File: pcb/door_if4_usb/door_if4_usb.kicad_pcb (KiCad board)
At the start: 4 copper layers, 90 x 45 mm, 117 parts, among them J1 WAGO 250-206, J2 WAGO 250-206, J3 WAGO 250-206, Q1 IRF7343, Q2 IRF7343, Q3 IRF7343, Q4 IRF7343, Q5 IRF7343, Q6 IRF7343, U1 Pico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

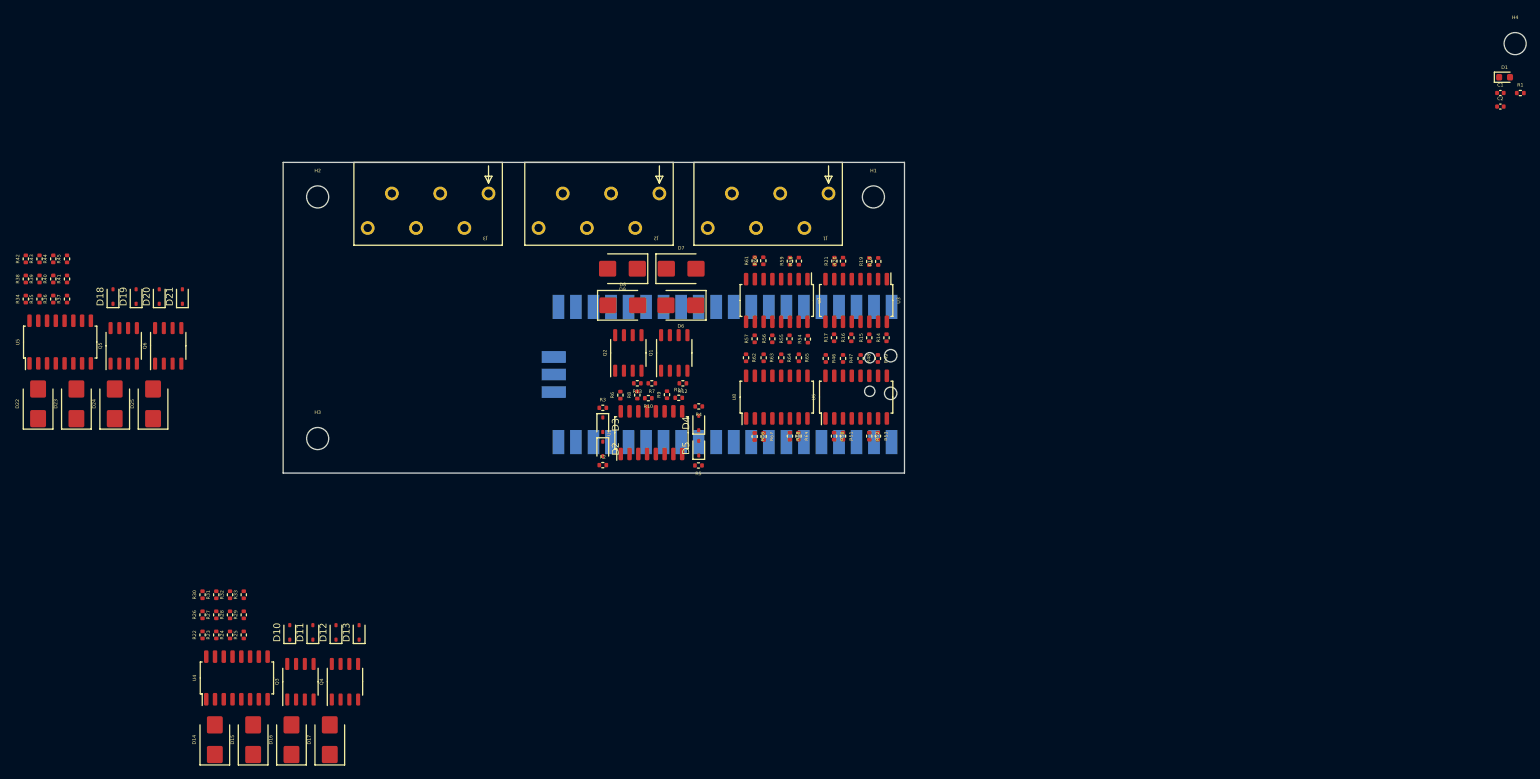
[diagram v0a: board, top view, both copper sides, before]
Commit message: almost completed door_if4_usb for manufacturing
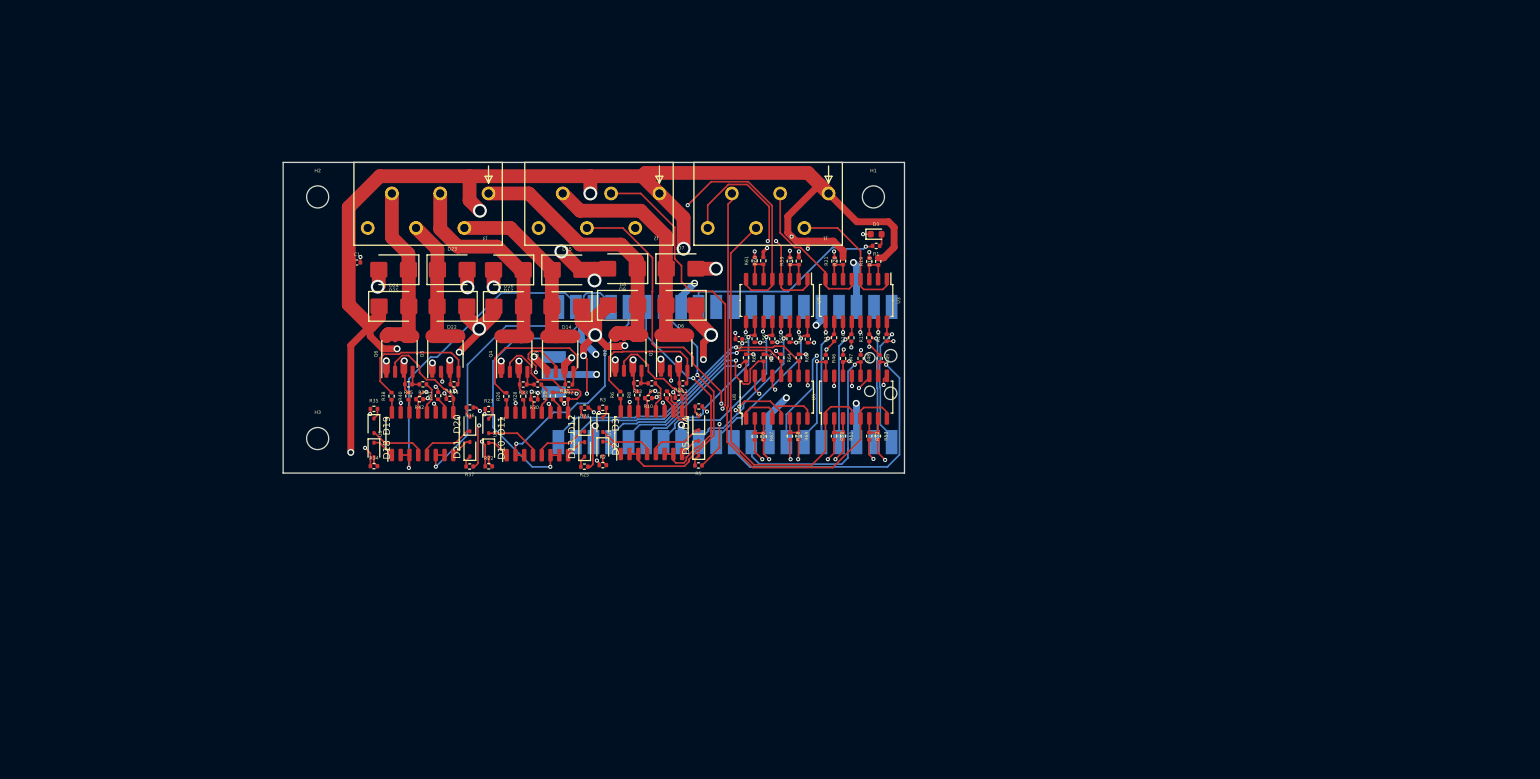
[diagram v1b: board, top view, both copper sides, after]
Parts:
- removed H4: MountingHole, MountingHole:MountingHole_3.2mm_M3_DIN965
- moved C1 167.4 mm to (70.7, 104.5)
- moved C2 115.3 mm to (126.0, 115.6), turned to 180 degrees
- moved R1 95.9 mm to (145.9, 102.1), turned to 180 degrees
- moved D1 93.8 mm to (145.9, 100.4)
- moved D15 81.8 mm to (101.1, 105.6), turned to 0 degrees
- moved D14 80.8 mm to (101.1, 110.9), turned to 180 degrees
- moved D17 72.8 mm to (92.6, 105.6), turned to 180 degrees
- moved D16 70.2 mm to (92.7, 110.9), turned to 0 degrees
- moved R37 63.2 mm to (87.0, 134.1), turned to 180 degrees
- moved R43 62.8 mm to (84.2, 124.2), turned to 0 degrees
- moved R36 62.4 mm to (87.0, 125.5), turned to 180 degrees
- moved D22 61.6 mm to (84.5, 110.8), turned to 180 degrees
- moved R24 61.0 mm to (103.7, 125.5), turned to 180 degrees
- moved R44 60.8 mm to (84.8, 122.2), turned to 180 degrees
- moved Q3 60.6 mm to (100.1, 117.8)
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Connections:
- U3 pad 11: Net-(U3-Pad11) -> GND
- U3 pad 13: Net-(U3-Pad11) -> GND
- U3 pad 15: Net-(U3-Pad11) -> GND
- U3 pad 9: Net-(U3-Pad11) -> GND
- U6 pad 11: Net-(U6-Pad11) -> GND
- U6 pad 13: Net-(U6-Pad11) -> GND
- U6 pad 15: Net-(U6-Pad11) -> GND
- U6 pad 9: Net-(U6-Pad11) -> GND
- U7 pad 11: Net-(U7-Pad11) -> GND
- U7 pad 13: Net-(U7-Pad11) -> GND
- U7 pad 15: Net-(U7-Pad11) -> GND
- U7 pad 9: Net-(U7-Pad11) -> GND
- U8 pad 11: Net-(U8-Pad11) -> GND
- U8 pad 13: Net-(U8-Pad11) -> GND
- U8 pad 15: Net-(U8-Pad11) -> GND
- U8 pad 9: Net-(U8-Pad11) -> GND
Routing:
- net +24V: track 0.00 -> 453.8 mm, vias 0 -> 30
- net GNDA: track 0.00 -> 161.8 mm, vias 0 -> 33
- net +3V3: track 0.00 -> 122.5 mm, vias 0 -> 22
- net GND: track 0.00 -> 91.4 mm, vias 0 -> 31
- net IN4: track 0.00 -> 68.2 mm
- net IN3: track 0.00 -> 59.7 mm
- net IN8: track 0.00 -> 55.7 mm, vias 0 -> 2
- net IN7: track 0.00 -> 52.9 mm, vias 0 -> 2
- net S_OUT4: track 0.00 -> 48.4 mm, vias 0 -> 1
- net S_OUT5: track 0.00 -> 47.4 mm, vias 0 -> 1
- net S_IN4B: track 0.00 -> 44.9 mm, vias 0 -> 1
- net S_IN8B: track 0.00 -> 43.2 mm, vias 0 -> 1
- net IN6: track 0.00 -> 40.9 mm, vias 0 -> 1
- net OUT2: track 0.00 -> 40.6 mm
- net S_IN8A: track 0.00 -> 37.6 mm, vias 0 -> 1
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- added copper zone on In1.Cu, net +3V3
- added copper zone on In2.Cu, net GND
- added copper zone on In1.Cu, net GNDA

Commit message: added final if4 design
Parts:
- added D26: D, Diode_SMD:D_SOD-523, F.Cu at (147.8, 104.2)
- added D27: D, Diode_SMD:D_SOD-523, F.Cu at (138.1, 129.8)
- added D28: D, Diode_SMD:D_SOD-523, F.Cu at (136.2, 104.2)
- added D29: D, Diode_SMD:D_SOD-523, F.Cu at (130.9, 129.8)
- added D30: D, Diode_SMD:D_SOD-523, F.Cu at (143.4, 104.3)
- added D31: D, Diode_SMD:D_SOD-523, F.Cu at (140.5, 129.2)
- added D32: D, Diode_SMD:D_SOD-523, F.Cu at (132.1, 104.2)
- added D33: D, Diode_SMD:D_SOD-523, F.Cu at (128.7, 129.2)
- added D34: D, Diode_SMD:D_SOD-523, F.Cu at (138.3, 103.8)
- added D35: D, Diode_SMD:D_SOD-523, F.Cu at (143.1, 130.0)
- added D36: D, Diode_SMD:D_SOD-523, F.Cu at (130.4, 104.2)
- added D37: D, Diode_SMD:D_SOD-523, F.Cu at (136.1, 129.8)
- added D38: D, Diode_SMD:D_SOD-523, F.Cu at (140.4, 105.0)
- added D39: D, Diode_SMD:D_SOD-523, F.Cu at (145.3, 129.2)
- added D40: D, Diode_SMD:D_SOD-523, F.Cu at (128.2, 104.9)
- added D41: D, Diode_SMD:D_SOD-523, F.Cu at (133.8, 129.3)
- C1, C2: footprint Capacitor_SMD:C_0402_1005Metric -> Capacitor_SMD:C_0805_2012Metric
- R18, R19, R20, R21, R50, R51, R52, R53, R58, R59, R60, R61, R66, R67, R68, R69: value 22k -> 10k
- moved C2 26.5 mm to (148.0, 130.4), turned to -90 degrees
- moved C1 4.55 mm to (66.8, 102.2), turned to 90 degrees
- moved R69 1.75 mm to (134.7, 131.4)
- moved R68 1.74 mm to (133.5, 131.4)
- moved R52 1.60 mm to (144.8, 131.2)
- moved R53 1.55 mm to (145.9, 131.2)
- moved R51 1.49 mm to (141.1, 131.1)
- moved R66 1.48 mm to (128.0, 131.2)
- moved R50 1.46 mm to (139.8, 131.1)
- moved R67 1.45 mm to (129.5, 131.2)
- moved R61 1.33 mm to (127.5, 103.2)
- moved R60 1.33 mm to (128.8, 103.2)
- moved R20 1.06 mm to (140.9, 103.2)
- moved R21 1.06 mm to (139.7, 103.2)
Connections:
- R18 pad 1: Net-(R18-Pad1) -> Net-(D30-A)
- R19 pad 1: Net-(R18-Pad1) -> Net-(D30-A)
- R20 pad 1: Net-(R20-Pad1) -> Net-(D38-A)
- R21 pad 1: Net-(R20-Pad1) -> Net-(D38-A)
- R50 pad 1: Net-(R50-Pad1) -> Net-(D31-A)
- R51 pad 1: Net-(R50-Pad1) -> Net-(D31-A)
- R52 pad 1: Net-(R52-Pad1) -> Net-(D39-A)
- R53 pad 1: Net-(R52-Pad1) -> Net-(D39-A)
- R58 pad 1: Net-(R58-Pad1) -> Net-(D32-A)
- R59 pad 1: Net-(R58-Pad1) -> Net-(D32-A)
- R60 pad 1: Net-(R60-Pad1) -> Net-(D40-A)
- R61 pad 1: Net-(R60-Pad1) -> Net-(D40-A)
- R66 pad 1: Net-(R66-Pad1) -> Net-(D33-A)
- R67 pad 1: Net-(R66-Pad1) -> Net-(D33-A)
- R68 pad 1: Net-(R68-Pad1) -> Net-(D41-A)
- R69 pad 1: Net-(R68-Pad1) -> Net-(D41-A)
- U3 pad 1: IN1 -> Net-(D26-K)
- U3 pad 2: Net-(R18-Pad1) -> Net-(D30-A)
- U3 pad 3: Net-(R18-Pad1) -> Net-(D30-K)
- U3 pad 5: IN2 -> Net-(D34-K)
- U3 pad 6: Net-(R20-Pad1) -> Net-(D38-A)
- U3 pad 7: Net-(R20-Pad1) -> Net-(D38-K)
- U6 pad 1: IN3 -> Net-(D27-K)
- U6 pad 2: Net-(R50-Pad1) -> Net-(D31-A)
- U6 pad 3: Net-(R50-Pad1) -> Net-(D31-K)
- U6 pad 5: IN4 -> Net-(D35-K)
- U6 pad 6: Net-(R52-Pad1) -> Net-(D39-A)
- U6 pad 7: Net-(R52-Pad1) -> Net-(D39-K)
- U7 pad 1: IN5 -> Net-(D28-K)
- U7 pad 2: Net-(R58-Pad1) -> Net-(D32-A)
- U7 pad 3: Net-(R58-Pad1) -> Net-(D32-K)
- U7 pad 5: IN6 -> Net-(D36-K)
- U7 pad 6: Net-(R60-Pad1) -> Net-(D40-A)
- U7 pad 7: Net-(R60-Pad1) -> Net-(D40-K)
- U8 pad 1: IN7 -> Net-(D29-K)
- U8 pad 2: Net-(R66-Pad1) -> Net-(D33-A)
- U8 pad 3: Net-(R66-Pad1) -> Net-(D33-K)
- U8 pad 5: IN8 -> Net-(D37-K)
- U8 pad 6: Net-(R68-Pad1) -> Net-(D41-A)
- U8 pad 7: Net-(R68-Pad1) -> Net-(D41-K)
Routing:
- net +3V3: track 122.5 -> 136.5 mm
- net Net-(D34-K): track 0.00 -> 9.28 mm
- net Net-(D37-K): track 0.00 -> 9.03 mm
- net Net-(D29-K): track 0.00 -> 8.68 mm
- net Net-(R60-Pad1): track 5.58 -> 0.00 mm
- net Net-(R58-Pad1): track 5.52 -> 0.00 mm
- net Net-(R66-Pad1): track 5.52 -> 0.00 mm
- net Net-(R20-Pad1): track 5.47 -> 0.00 mm
- net Net-(R18-Pad1): track 5.42 -> 0.00 mm
- net Net-(R50-Pad1): track 5.42 -> 0.00 mm
- net Net-(D30-A): track 0.00 -> 5.37 mm
- net Net-(R68-Pad1): track 5.37 -> 0.00 mm
- net Net-(R52-Pad1): track 5.37 -> 0.00 mm
- net Net-(D32-A): track 0.00 -> 5.33 mm
- net Net-(D41-A): track 0.00 -> 5.30 mm
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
